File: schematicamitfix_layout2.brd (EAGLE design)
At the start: 28 x 47 mm, 39 parts, among them J1 FTDI_DEVICE, M1 WIRELESS-NRF24L01, U1 ATMEGA328P_TQFP, U2 GY-521MPU6050, U3 MAX1595EUA33+, Y1 8MHz

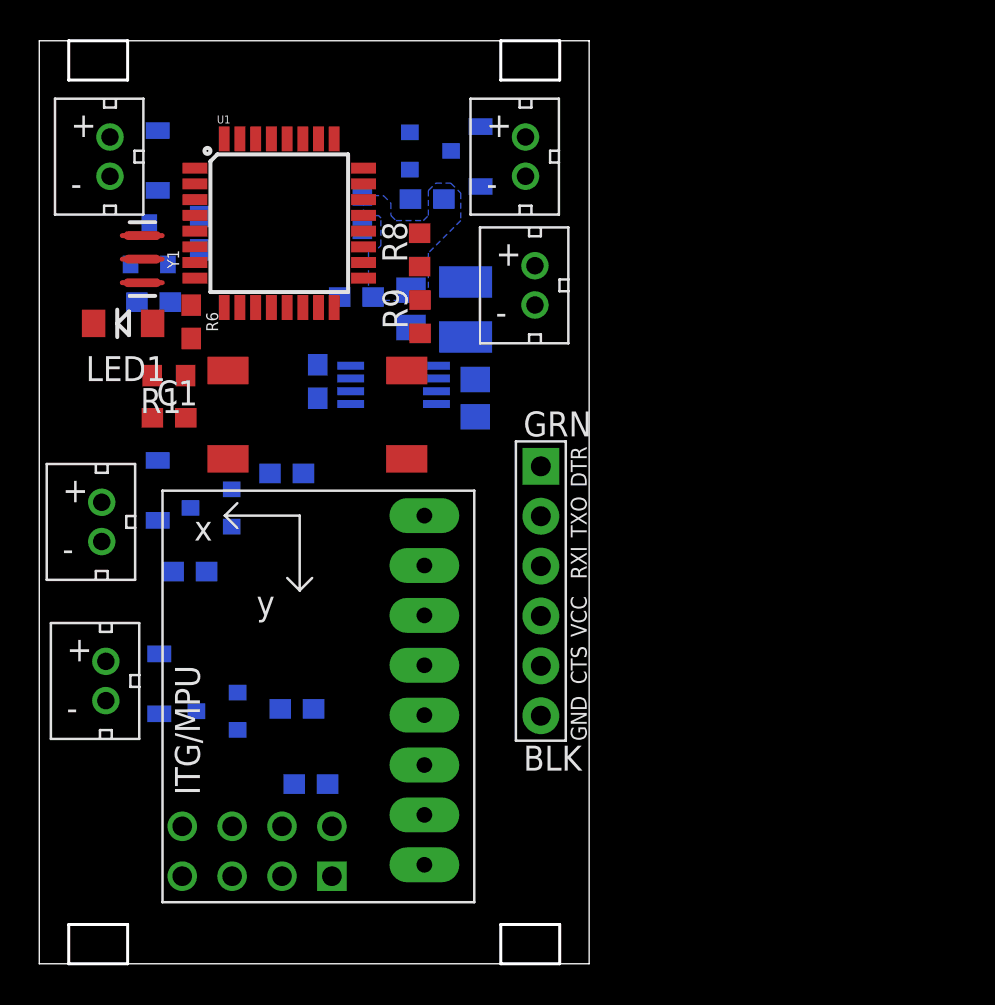
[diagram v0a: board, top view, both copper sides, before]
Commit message: Added layout3 (Plane Layout), and routed most of the board.  Outstanding issues remain.
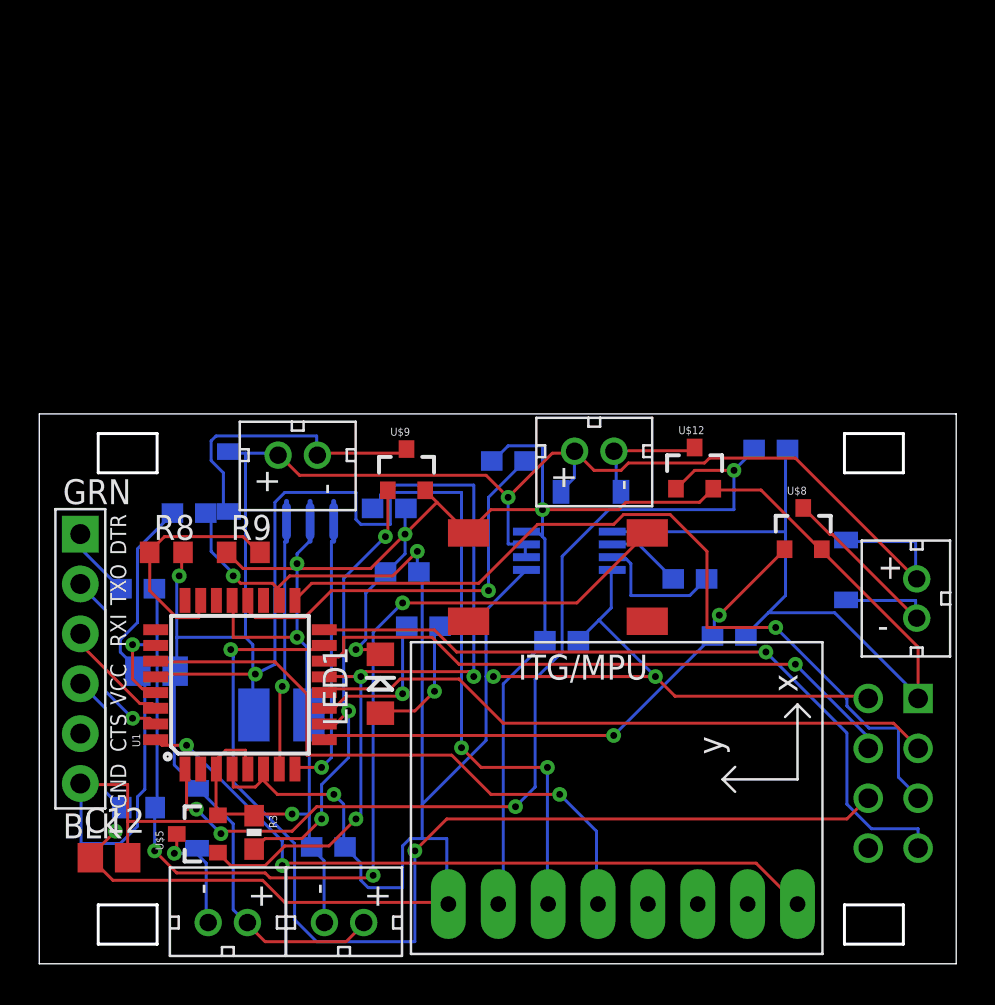
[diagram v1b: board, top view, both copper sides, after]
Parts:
- moved U$11 41.7 mm to (44.7, 18.6)
- moved U$15 39.5 mm to (9.60, 2.10), turned to 270 degrees
- moved U$10 35.3 mm to (41.1, 20.0)
- moved U$19 33.9 mm to (15.5, 2.10), turned to 270 degrees
- moved U$14 33.6 mm to (8.03, 7.38)
- moved C3 31.9 mm to (14.7, 5.95), turned to 0 degrees
- moved C12 31.9 mm to (3.55, 5.40), flipped to the top, turned to 0 degrees
- moved U$8 30.1 mm to (38.9, 22.1), flipped to the top, turned to 0 degrees
- moved U$5 30.1 mm to (8.10, 6.61), flipped to the top, turned to 90 degrees
- moved M1 25.5 mm to (32.0, 7.16), turned to 0 degrees
- moved R4 24.0 mm to (35.1, 16.7)
- moved J1 23.7 mm to (2.09, 15.5)
- moved U1 23.6 mm to (10.2, 14.2), turned to 90 degrees
- moved C13 22.7 mm to (12.3, 12.7), turned to 0 degrees
- moved LED1 22.5 mm to (17.4, 14.3), turned to 90 degrees
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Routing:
- net GND: track 0.00 -> 183.0 mm, vias 0 -> 6
- net VCC: track 0.00 -> 125.0 mm, vias 0 -> 6
- net VIN: track 0.00 -> 96.6 mm, vias 0 -> 2
- net N$1: track 0.00 -> 58.1 mm, vias 0 -> 4
- net NRF_MOSI: track 0.00 -> 55.4 mm, vias 0 -> 2
- net IMU_SCL: track 0.00 -> 52.0 mm, vias 0 -> 3
- net PWM1: track 0.00 -> 50.2 mm, vias 0 -> 4
- net NRF_SCK: track 0.00 -> 43.5 mm, vias 0 -> 1
- net PWM4: track 0.00 -> 39.0 mm, vias 0 -> 3
- net NRF_MISO: track 0.00 -> 37.5 mm, vias 0 -> 1
- net IMU_INT: track 0.00 -> 37.0 mm, vias 0 -> 2
- net NRF_CE: track 0.00 -> 32.0 mm
- net IMU_SDA: track 0.00 -> 31.6 mm, vias 0 -> 1
- net NRF_CSN: track 0.00 -> 31.3 mm, vias 0 -> 1
- net PWM3: track 0.00 -> 27.9 mm, vias 0 -> 2
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- removed copper zone on layer 16, net N$3
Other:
- board size 28 x 47 mm -> 46.7 x 28 mm
